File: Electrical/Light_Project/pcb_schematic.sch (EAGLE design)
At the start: 9 parts, among them U1 REG710NA-3.3/3K, U2 ATTINY85V-10SU

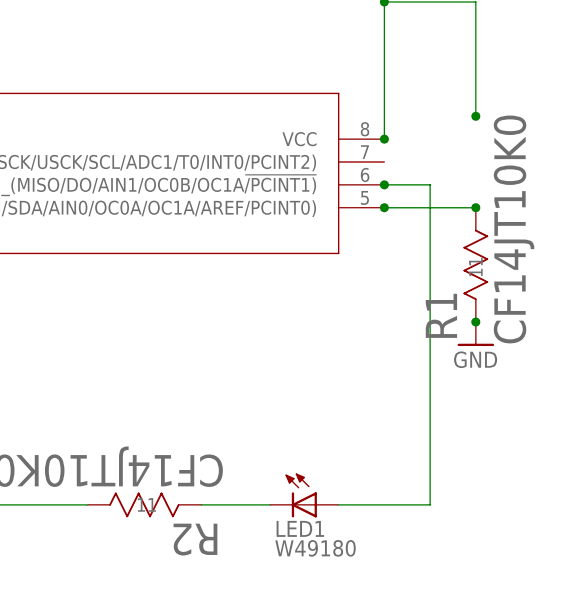
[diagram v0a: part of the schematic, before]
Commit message: Route PCB (not optimized)
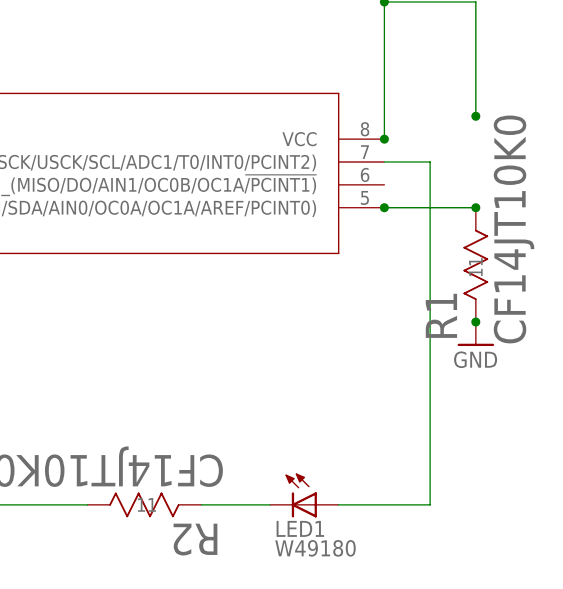
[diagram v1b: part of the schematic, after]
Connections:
- net N$7: now also U2.PB2_(SCK/USCK/SCL/ADC1/T0/INT0/PCINT2); no longer U2.PB1_(MISO/DO/AIN1/OC0B/OC1A!/PCINT1)
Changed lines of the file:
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@@
 <pinref part="LED1" gate="G$1" pin="A"/>
 <wire x1="213.36" y1="-45.72" x2="223.52" y2="-45.72" width="0.1524" layer="91"/>
-<wire x1="223.52" y1="-45.72" x2="223.52" y2="-10.16" width="0.1524" layer="91"/>
-<pinref part="U2" gate="A" pin="PB1_(MISO/DO/AIN1/OC0B/OC1A!/PCINT1)"/>
-<wire x1="223.52" y1="-10.16" x2="218.44" y2="-10.16" width="0.1524" layer="91"/>
-<junction x="218.44" y="-10.16"/>
+<wire x1="223.52" y1="-45.72" x2="223.52" y2="-7.62" width="0.1524" layer="91"/>
+<pinref part="U2" gate="A" pin="PB2_(SCK/USCK/SCL/ADC1/T0/INT0/PCINT2)"/>
+<wire x1="218.44" y1="-7.62" x2="223.52" y2="-7.62" width="0.1524" layer="91"/>
 </segment>
 </net>
